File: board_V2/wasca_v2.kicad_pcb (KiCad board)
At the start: 2 copper layers, 63 parts, among them CN1 CARTRIDGE_EDGE_CONNECTOR, CON1 SnickerDoodle, CON2 SD_Card, U1 74ALVC164245, U10 M24C04-WDW6TP, U11 TXS0108EPWR, U13 M24C04-WDW6TP, U2 74ALVC164245, U3 74ALVC164245, U4 74LVC1T45GW,125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

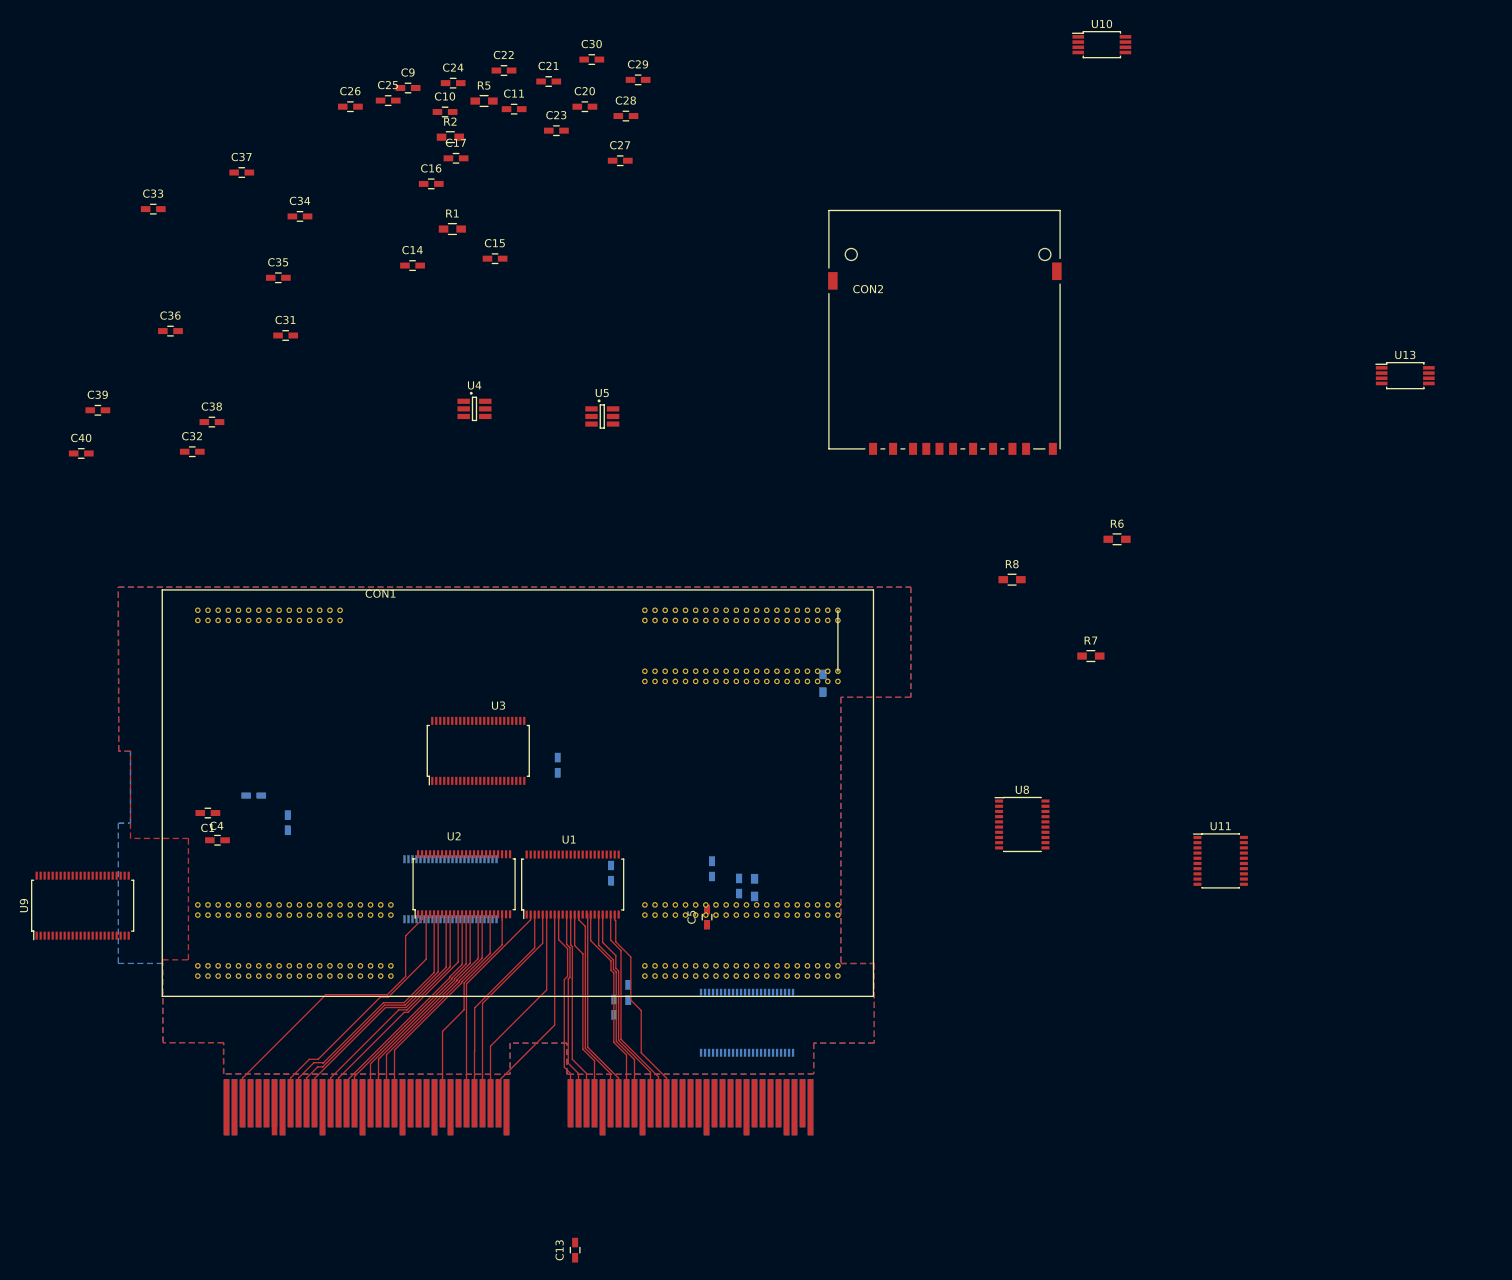
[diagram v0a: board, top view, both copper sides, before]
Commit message: Schematic update, SPI display added
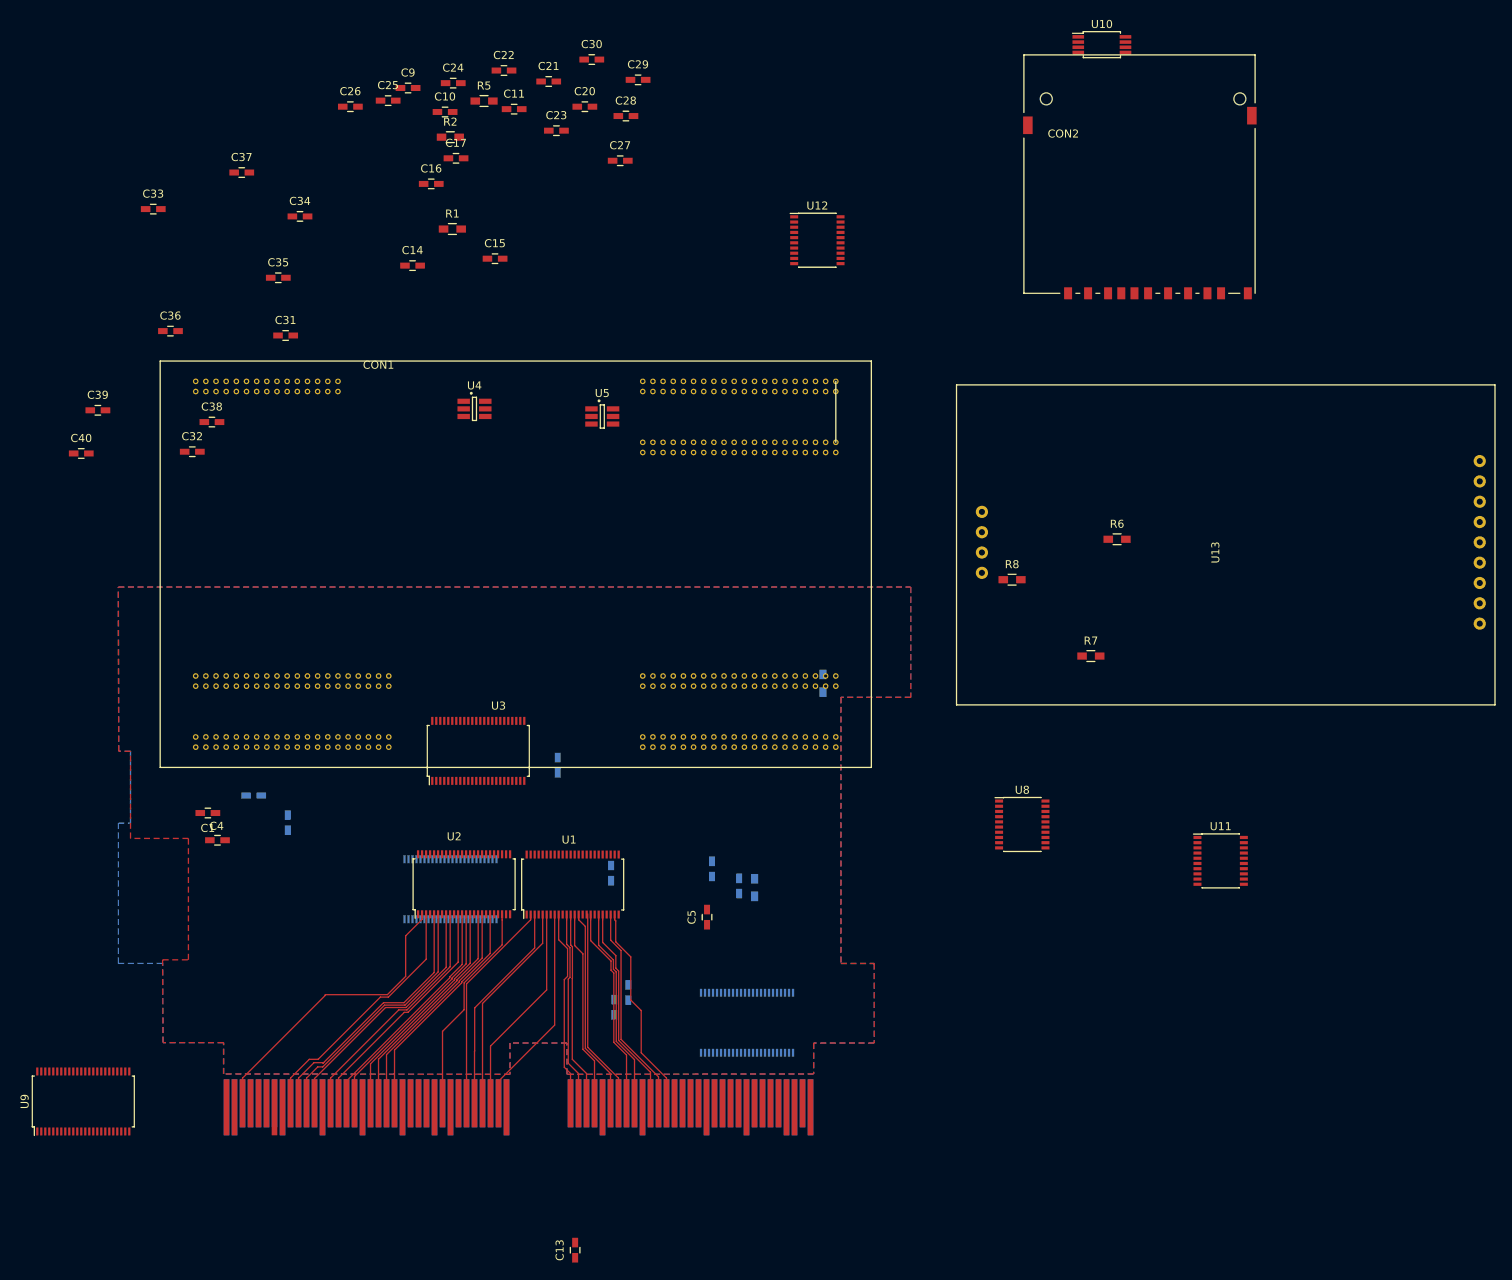
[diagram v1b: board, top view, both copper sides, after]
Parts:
- added U12: TXS0108EPWR, Housings_SSOP:SSOP-20_4.4x6.5mm_Pitch0.65mm, F.Cu at (114.7, 45.4)
- U13: value M24C04-WDW6TP -> ILI9341_LCD_Breakout; footprint Housings_SSOP:TSSOP-8_4.4x3mm_Pitch0.65mm -> wasca:ILI9341_LCD_Breakout
- moved U13 42.7 mm to (199.4, 103.5), turned to 90 degrees
- moved CON2 31.2 mm to (155.4, 52.0)
- moved CON1 28.6 mm to (77.0, 87.2)
- moved U9 24.5 mm to (22.9, 153.1)
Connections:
- C36 pad 1: /+3_3V -> /+1_8V
- CON1 pad B23: Net-(CON1-PadB23) -> /SPI_SCK_1_8V
- CON1 pad B24: Net-(CON1-PadB24) -> /SPI_CS1_1_8V
- CON1 pad B25: Net-(CON1-PadB25) -> /SPI_MISO_1_8V
- CON1 pad B26: Net-(CON1-PadB26) -> /SPI_CS0_1_8V
- CON1 pad B29: Net-(CON1-PadB29) -> /SPI_CS2_1_8V
- CON1 pad B30: Net-(CON1-PadB30) -> /LCD_RESET_1_8V
- CON1 pad B31: Net-(CON1-PadB31) -> /SPI_MOSI_1_8V
- CON1 pad B32: Net-(CON1-PadB32) -> /LCD_DC_1_8V
- CON1 pad B35: Net-(CON1-PadB35) -> /LCD_LED_1_8V
- U11 pad 12: Net-(U11-Pad12) -> /LCD_LED
- U11 pad 9: Net-(U11-Pad9) -> /LCD_LED_1_8V
- U13 pad 1: GND -> /+3_3V
- U13 pad 3: GND -> /SPI_CS0
- U13 pad 4: GND -> /LCD_RESET
- U13 pad 5: Net-(CON2-PadC40) -> /LCD_DC
- U13 pad 6: Net-(CON2-PadC39) -> /SPI_MOSI
- U13 pad 7: Net-(R6-Pad2) -> /SPI_SCK
- U13 pad 8: /+3_3V -> /LCD_LED

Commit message: Pin swapping (incomplete)
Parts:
- CON1, CON2: moved to B.Cu
- moved U13 160.1 mm to (44.0, 65.0), turned to 270 degrees
- moved U10 149.3 mm to (34.8, 115.5), turned to 90 degrees
- moved U11 96.3 mm to (79.3, 79.2), turned to 270 degrees
- moved U12 85.9 mm to (38.5, 85.0)
- moved CON2 84.3 mm to (79.9, 89.3), turned to 0 degrees
- moved U8 68.9 mm to (71.8, 125.6), turned to 270 degrees
- moved U4 68.2 mm to (99.3, 128.9), turned to 270 degrees
- moved C13 62.8 mm to (123.4, 122.4)
- moved U5 57.1 mm to (100.4, 123.1), turned to 270 degrees
- moved C8 52.9 mm to (142.1, 137.0)
- moved C18 48.8 mm to (131.0, 108.7)
- moved R4 47.5 mm to (147.4, 135.8)
- moved C7 42.2 mm to (130.9, 120.2)
- moved C2 38.1 mm to (129.1, 142.0)
- moved C12 38.0 mm to (139.0, 130.6)
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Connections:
- CON1 pad E11: /ABUS_A11_3V -> /ABUS_D9_3V
- CON1 pad E12: /EXBG22_3V -> /ABUS_D4_3V
- CON1 pad E13: /ABUS_A10_3V -> /ABUS_D8_3V
- CON1 pad E14: /ABUS_D0_3V -> /ABUS_D15_3V
- CON1 pad E17: /ABUS_A1_3V -> /ABUS_D3_3V
- CON1 pad E18: /ABUS_D1_3V -> /ABUS_D14_3V
- CON1 pad E19: /ABUS_CS0_3V -> /ABUS_D2_3V
- CON1 pad E20: /ABUS_D2_3V -> /ABUS_D13_3V
- CON1 pad E23: /ABUS_CS2_3V -> /ABUS_D1_3V
- CON1 pad E24: /ABUS_D3_3V -> /ABUS_D12_3V
- CON1 pad E25: /ABUS_WR0_3V -> /ABUS_D0_3V
- CON1 pad E26: /ABUS_D8_3V -> /EXBG20_3V
- CON1 pad E29: /SSEL_3V -> /ABUS_IRQ_DIR
- CON1 pad E30: /ABUS_D9_3V -> /EXBG16_3V
- CON1 pad E31: /ABUS_DATA_DIR -> /ABUS_IRQ_3V
- CON1 pad E32: /ABUS_D10_3V -> /EXBG18_3V
- CON1 pad E36: /ABUS_D11_3V -> /EXBG22_3V
- CON1 pad E37: /ABUS_IRQ_DIR -> /ABUS_WAIT_3V
- CON1 pad E38: /ABUS_D7_3V -> /SSEL_3V
- CON1 pad E4: /EXBG16_3V -> /ABUS_D7_3V
- CON1 pad E5: /ABUS_A8_3V -> /ABUS_D11_3V
- CON1 pad E6: /EXBG18_3V -> /ABUS_D6_3V
- CON1 pad E7: /ABUS_A9_3V -> /ABUS_D10_3V
- CON1 pad E8: /EXBG20_3V -> /ABUS_D5_3V
- CON1 pad F12: /ABUS_D15_3V -> /ABUS_A10_3V
- CON1 pad F14: /ABUS_D14_3V -> /ABUS_A1_3V
- CON1 pad F18: /ABUS_D13_3V -> /ABUS_CS0_3V
- CON1 pad F20: /ABUS_D12_3V -> /ABUS_CS2_3V
- CON1 pad F24: /ABUS_WAIT_3V -> /ABUS_WR0_3V
- CON1 pad F26: /ABUS_IRQ_3V -> /ABUS_DATA_DIR
- CON1 pad F4: /ABUS_D6_3V -> /ABUS_A8_3V
- CON1 pad F6: /ABUS_D5_3V -> /ABUS_A9_3V
- CON1 pad F8: /ABUS_D4_3V -> /ABUS_A11_3V
- U6 pad 11: /ABUS_A12 -> /ABUS_A9
- U6 pad 12: /ABUS_A13 -> /ABUS_A8
- U6 pad 13: /ABUS_A8 -> /ABUS_A13
- U6 pad 14: /ABUS_A9 -> /ABUS_A12
- U6 pad 16: /ABUS_A11 -> /ABUS_A15
- U6 pad 17: /ABUS_A10 -> /ABUS_A17
- U6 pad 19: /ABUS_A1 -> /ABUS_A19
- U6 pad 2: /ABUS_A25 -> /ABUS_WR0
- U6 pad 20: /ABUS_CS0 -> /ABUS_A21
- U6 pad 22: /ABUS_CS2 -> /ABUS_A23
- U6 pad 23: /ABUS_WR0 -> /ABUS_A25
- U6 pad 26: /ABUS_WR0_3V -> /ABUS_A25_3V
- U6 pad 27: /ABUS_CS2_3V -> /ABUS_A23_3V
- U6 pad 29: /ABUS_CS0_3V -> /ABUS_A21_3V
- U6 pad 3: /ABUS_A23 -> /ABUS_CS2
- U6 pad 30: /ABUS_A1_3V -> /ABUS_A19_3V
- U6 pad 32: /ABUS_A10_3V -> /ABUS_A17_3V
- U6 pad 33: /ABUS_A11_3V -> /ABUS_A15_3V
- U6 pad 35: /ABUS_A9_3V -> /ABUS_A12_3V
- U6 pad 36: /ABUS_A8_3V -> /ABUS_A13_3V
- U6 pad 37: /ABUS_A13_3V -> /ABUS_A8_3V
- U6 pad 38: /ABUS_A12_3V -> /ABUS_A9_3V
- U6 pad 40: /ABUS_A15_3V -> /ABUS_A11_3V
- U6 pad 41: /ABUS_A17_3V -> /ABUS_A10_3V
- U6 pad 43: /ABUS_A19_3V -> /ABUS_A1_3V
- U6 pad 44: /ABUS_A21_3V -> /ABUS_CS0_3V
- U6 pad 46: /ABUS_A23_3V -> /ABUS_CS2_3V
- U6 pad 47: /ABUS_A25_3V -> /ABUS_WR0_3V
- U6 pad 5: /ABUS_A21 -> /ABUS_CS0
- U6 pad 6: /ABUS_A19 -> /ABUS_A1
- U6 pad 8: /ABUS_A17 -> /ABUS_A10
- U6 pad 9: /ABUS_A15 -> /ABUS_A11
- U7 pad 11: /EXBG4 -> /EXBG10
- U7 pad 12: /EXBG6 -> /EXBG8
- U7 pad 13: /EXBG8 -> /EXBG6
- U7 pad 14: /EXBG10 -> /EXBG4
- U7 pad 16: /EXBG12 -> /EXBG2
- U7 pad 17: /EXBG14 -> /EXBG0
- U7 pad 19: /EXBG16 -> Net-(U7-Pad19)
- U7 pad 2: /ISD -> /EXBG22
- U7 pad 20: /EXBG18 -> /ILRCK
- U7 pad 22: /EXBG20 -> /IBCK
- U7 pad 23: /EXBG22 -> /ISD
- U7 pad 26: /EXBG22_3V -> /ISD_3V
- U7 pad 27: /EXBG20_3V -> /IBCK_3V
- U7 pad 29: /EXBG18_3V -> /ILRCK_3V
- U7 pad 3: /IBCK -> /EXBG20
- U7 pad 30: /EXBG16_3V -> Net-(U7-Pad30)
- U7 pad 32: /EXBG14_3V -> /EXBG0_3V
- U7 pad 33: /EXBG12_3V -> /EXBG2_3V
- U7 pad 35: /EXBG10_3V -> /EXBG4_3V
- U7 pad 36: /EXBG8_3V -> /EXBG6_3V
- U7 pad 37: /EXBG6_3V -> /EXBG8_3V
- U7 pad 38: /EXBG4_3V -> /EXBG10_3V
- U7 pad 40: /EXBG2_3V -> /EXBG12_3V
- U7 pad 41: /EXBG0_3V -> /EXBG14_3V
- U7 pad 43: Net-(U7-Pad43) -> /EXBG16_3V
- U7 pad 44: /ILRCK_3V -> /EXBG18_3V
- U7 pad 46: /IBCK_3V -> /EXBG20_3V
- U7 pad 47: /ISD_3V -> /EXBG22_3V
- U7 pad 5: /ILRCK -> /EXBG18
- U7 pad 6: Net-(U7-Pad6) -> /EXBG16
- U7 pad 8: /EXBG0 -> /EXBG14
- U7 pad 9: /EXBG2 -> /EXBG12
- U9 pad 20: /MCLK -> Net-(U9-Pad20)
- U9 pad 22: /COPRO_RST -> Net-(U9-Pad22)
- U9 pad 27: /COPRO_RST_3V -> Net-(U9-Pad27)
- U9 pad 29: /MCLK_3V -> Net-(U9-Pad29)
- U9 pad 3: Net-(U9-Pad3) -> /MCLK
- U9 pad 44: Net-(U9-Pad44) -> /COPRO_RST_3V
- U9 pad 46: Net-(U9-Pad46) -> /MCLK_3V
- U9 pad 5: Net-(U9-Pad5) -> /COPRO_RST
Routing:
- net GND: track 0.00 -> 247.4 mm, vias 0 -> 25
- net /+5V: track 0.00 -> 109.3 mm, vias 0 -> 8
- net /COPRO_RST: track 0.00 -> 104.1 mm, vias 0 -> 1
- net /MCLK: track 0.00 -> 100.9 mm, vias 0 -> 2
- net /ABUS_WR0_3V: track 0.00 -> 78.5 mm
- net /ABUS_CS2_3V: track 0.00 -> 73.7 mm
- net /ABUS_CS0_3V: track 0.00 -> 69.8 mm
- net /ABUS_A1_3V: track 0.00 -> 64.6 mm
- net /ABUS_A10_3V: track 0.00 -> 59.8 mm
- net /ABUS_A11_3V: track 0.00 -> 55.1 mm
- net /ABUS_A9_3V: track 0.00 -> 54.4 mm
- net /ABUS_D12_3V: track 0.00 -> 53.1 mm
- net /DOTCLK: track 0.00 -> 52.2 mm, vias 0 -> 1
- net /ABUS_A8_3V: track 0.00 -> 48.9 mm
- net /ABUS_D13_3V: track 0.00 -> 48.9 mm
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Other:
- rule pad_to_mask_clearance: 0.254 -> 0.1

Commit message: Almost routed
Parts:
- removed C39: 0.1uF, Capacitors_SMD:C_0603_HandSoldering
- removed C40: 10uF, Capacitors_SMD:C_0603_HandSoldering
- C12, C19, C2, C3, C6, C7, C8: moved to F.Cu
- C13, C15, C16, C31, C32, C38, R1, R2, R5: moved to B.Cu
- moved R6 124.6 mm to (30.4, 109.2), turned to 90 degrees
- moved R7 118.8 mm to (30.3, 104.5), turned to 90 degrees
- moved R8 111.8 mm to (30.4, 114.3), turned to 270 degrees
- moved C20 109.7 mm to (41.8, 129.3), turned to 90 degrees
- moved C9 103.3 mm to (85.7, 127.3), turned to 90 degrees
- moved C10 100.5 mm to (57.8, 129.4), turned to 90 degrees
- moved C25 99.8 mm to (116.8, 110.8), turned to 270 degrees
- moved C16 98.6 mm to (102.9, 129.9)
- moved C17 98.5 mm to (74.7, 133.5), turned to 270 degrees
- moved C11 97.1 mm to (96.7, 124.1), turned to 90 degrees
- moved C15 93.8 mm to (51.3, 138.6), turned to 270 degrees
- moved C19 91.1 mm to (43.8, 142.8), turned to 0 degrees
- moved C22 87.4 mm to (119.4, 99.8), turned to 90 degrees
- moved C3 86.9 mm to (110.9, 129.8)
- moved R4 86.4 mm to (71.8, 94.0), turned to 90 degrees
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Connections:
- C28 pad 1: Net-(C28-Pad1) -> /+5V
- C30 pad 1: Net-(C30-Pad1) -> /+5V
- CON1 pad C11: /ABUS_A20_3V -> /EXBG15_3V
- CON1 pad C12: /EXBG5_3V -> /EXBG13_3V
- CON1 pad C13: /ABUS_A18_3V -> /EXBG11_3V
- CON1 pad C14: /EXBG7_3V -> /EXBG9_3V
- CON1 pad C17: /ABUS_A16_3V -> /EXBG7_3V
- CON1 pad C18: /EXBG9_3V -> /EXBG5_3V
- CON1 pad C19: /ABUS_A14_3V -> /EXBG3_3V
- CON1 pad C20: /EXBG11_3V -> /EXBG1_3V
- CON1 pad C23: /ABUS_A7_3V -> /SSEL_3V
- CON1 pad C24: /EXBG13_3V -> /EXSL_3V
- CON1 pad C25: /ABUS_A6_3V -> /SCSPCLK_3V
- CON1 pad C26: /EXBG15_3V -> /RESET_3V
- CON1 pad C29: /ABUS_A5_3V -> /DLRCLK_3V
- CON1 pad C30: /EXBG17_3V -> /DBCK_3V
- CON1 pad C31: /ABUS_A4_3V -> /DSD_3V
- CON1 pad C32: /EXBG19_3V -> /VSYNC_3V
- CON1 pad C35: /ABUS_A3_3V -> /HSYNC_3V
- CON1 pad C36: /EXBG21_3V -> /COPRO_RST_3V
- CON1 pad C37: /ABUS_A2_3V -> /MCLK_3V
- CON1 pad C4: /EXBG23_3V -> /EXLAT_3V
- CON1 pad C5: /ABUS_A24_3V -> /EXBG23_3V
- CON1 pad C6: /EXBG1_3V -> /EXBG21_3V
- CON1 pad C7: /ABUS_A22_3V -> /EXBG19_3V
- CON1 pad C8: /EXBG3_3V -> /EXBG17_3V
- CON1 pad D11: /ABUS_CS1_3V -> /EXBG22_3V
- CON1 pad D12: /IBCK_3V -> Net-(CON1-PadD12)
- CON1 pad D13: /ABUS_WR1_3V -> /EXBG18_3V
- CON1 pad D14: /ILRCK_3V -> /EXBG20_3V
- CON1 pad D17: /ABUS_A25_3V -> /EXBG14_3V
- CON1 pad D18: /EXBG0_3V -> /EXBG16_3V
- CON1 pad D19: /ABUS_A23_3V -> /EXBG10_3V
- CON1 pad D20: /EXBG2_3V -> /EXBG12_3V
- CON1 pad D23: /ABUS_A21_3V -> /EXBG6_3V
- CON1 pad D24: /EXBG4_3V -> /EXBG8_3V
- CON1 pad D25: /ABUS_A19_3V -> /EXBG2_3V
- CON1 pad D26: /EXBG6_3V -> /EXBG4_3V
- CON1 pad D29: /ABUS_A17_3V -> /EXBG0_3V
- CON1 pad D30: /EXBG8_3V -> /CRTG1_3V
- CON1 pad D31: /ABUS_A15_3V -> /ILRCK_3V
- CON1 pad D32: /EXBG10_3V -> /CRTG0_3V
- CON1 pad D35: /ABUS_A12_3V -> /IBCK_3V
- CON1 pad D36: /EXBG12_3V -> /EXON_3V
- CON1 pad D37: /ABUS_A13_3V -> /ISD_3V
- CON1 pad D38: /EXBG14_3V -> /MPEGON_3V
- CON1 pad D4: /EXLAT_3V -> /ABUS_DATA_DIR
- CON1 pad D5: /ABUS_A0_3V -> /ABUS_A24_3V
- CON1 pad D7: /ABUS_RD_3V -> /ABUS_A22_3V
- CON1 pad D8: /ISD_3V -> Net-(CON1-PadD8)
- CON1 pad E26: /EXBG20_3V -> /ABUS_A2_3V
- CON1 pad E30: /EXBG16_3V -> /ABUS_A0_3V
- CON1 pad E32: /EXBG18_3V -> /ABUS_RD_3V
- CON1 pad E36: /EXBG22_3V -> /ABUS_CS1_3V
- CON1 pad E38: /SSEL_3V -> /ABUS_WR1_3V
- CON1 pad F11: /HSYNC_3V -> /ABUS_A15_3V
- CON1 pad F13: /VSYNC_3V -> /ABUS_A17_3V
- CON1 pad F17: /DSD_3V -> /ABUS_A19_3V
- CON1 pad F19: /DBCK_3V -> /ABUS_A21_3V
- CON1 pad F23: /DLRCLK_3V -> /ABUS_A23_3V
- CON1 pad F25: /RESET_3V -> /ABUS_A25_3V
- CON1 pad F26: /ABUS_DATA_DIR -> /ABUS_A20_3V
- CON1 pad F29: /SCSPCLK_3V -> /ABUS_A3_3V
- CON1 pad F30: /MPEGON_3V -> /ABUS_A18_3V
- CON1 pad F31: /MCLK_3V -> /ABUS_A4_3V
- CON1 pad F32: /EXON_3V -> /ABUS_A16_3V
- CON1 pad F35: /COPRO_RST_3V -> /ABUS_A5_3V
- CON1 pad F36: /CRTG0_3V -> /ABUS_A14_3V
- CON1 pad F37: /EXSL_3V -> /ABUS_A6_3V
- CON1 pad F38: /CRTG1_3V -> /ABUS_A7_3V
- CON1 pad F5: Net-(CON1-PadF5) -> /ABUS_A13_3V
- CON1 pad F7: Net-(CON1-PadF7) -> /ABUS_A12_3V
- U12 pad 1: /SPI_SCK_1_8V -> /SPI_MOSI_1_8V
- U12 pad 12: /LCD_DC -> /SPI_SCK
- U12 pad 13: /SPI_CS0 -> /SPI_CS1
- U12 pad 14: /SPI_CS1 -> /SPI_MISO
- U12 pad 15: /SPI_MOSI -> /SPI_CS0
- U12 pad 16: /SPI_CS2 -> /LCD_RESET
- U12 pad 17: /LCD_RESET -> /SPI_CS2
- U12 pad 18: /SPI_MISO -> /SPI_MOSI
- U12 pad 20: /SPI_SCK -> /LCD_DC
- U12 pad 3: /SPI_MISO_1_8V -> /LCD_DC_1_8V
- U12 pad 6: /SPI_MOSI_1_8V -> /SPI_CS0_1_8V
- U12 pad 7: /SPI_CS1_1_8V -> /SPI_MISO_1_8V
- U12 pad 8: /SPI_CS0_1_8V -> /SPI_CS1_1_8V
- U12 pad 9: /LCD_DC_1_8V -> /SPI_SCK_1_8V
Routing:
- net /+3_3V: track 0.00 -> 405.6 mm, vias 0 -> 21
- net /+5V: track 109.3 -> 360.6 mm, vias 8 -> 23
- net GND: track 247.4 -> 353.4 mm, vias 25 -> 59
- net /ABUS_DATA_DIR: track 14.3 -> 93.7 mm, vias 0 -> 3
- net /+1_8V: track 0.00 -> 76.5 mm
- net /MPEGON_3V: track 0.00 -> 58.8 mm
- net /ABUS_A20_3V: track 0.00 -> 56.6 mm
- net /EXON_3V: track 0.00 -> 55.6 mm
- net /ABUS_A18_3V: track 0.00 -> 52.1 mm
- net /CRTG0_3V: track 0.00 -> 51.4 mm
- net /SD_DAT2_1_8V: track 0.00 -> 49.4 mm, vias 0 -> 1
- net /SD_CMD_1_8V: track 0.00 -> 48.5 mm, vias 0 -> 1
- net /SD_CLK_1_8V: track 0.00 -> 48.2 mm
- net /CRTG1_3V: track 0.00 -> 47.6 mm
- net /ABUS_A16_3V: track 0.00 -> 47.0 mm
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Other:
- net class POWER added: clearance 0.15, trace_width 0.4, via_dia 0.7, via_drill 0.3

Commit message: Route done
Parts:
- added G***: LOGO, wasca:Segata_Sanshiro, F.Cu at (120.7, 79.2)
- moved CON1 51.8 mm to (121.2, 59.9)
- moved C30 2.94 mm to (120.5, 60.6), turned to 0 degrees
- moved C26 1.23 mm to (32.5, 61.6), turned to 180 degrees
- moved C22 1.17 mm to (118.2, 99.5)
- moved C23 0.50 mm to (62.4, 107.3)
- moved C21 0.39 mm to (35.3, 62.9)
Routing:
- net GND: track 353.4 -> 685.9 mm, vias 59 -> 153
- net /SD_WP_1_8V: track 39.6 -> 43.5 mm
- net /+3_3V: track 405.6 -> 409.3 mm
- net /+1_8V: track 76.5 -> 79.3 mm
- net /SD_DAT2_1_8V: track 49.4 -> 51.9 mm
- net /EXBG10: track 19.0 -> 21.3 mm
- net /ABUS_A25_3V: track 40.1 -> 42.2 mm
- net /COPRO_RST_3V: track 26.5 -> 28.4 mm
- net /+5V: track 360.6 -> 358.9 mm
- net /ABUS_D15_3V: track 42.5 -> 44.1 mm
- net /ABUS_A22_3V: track 45.4 -> 46.8 mm
- net /SD_CD/DAT3_1_8V: track 46.7 -> 48.1 mm
- net /ABUS_A11_3V: track 55.3 -> 56.6 mm
- net /ABUS_D4_3V: track 39.8 -> 40.9 mm
- net /ABUS_A21_3V: track 41.1 -> 42.1 mm
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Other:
- board text added: "WASCA V 2.0"
